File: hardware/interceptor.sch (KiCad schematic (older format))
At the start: 23 parts, among them IC1 ATMEGA1284P-P, P1 TAPEPORT, P2 CIA1, P3 KEYBOARD, P4 OUTPUT, U1 7400, U2 ICL7660, U3 4520, U4 4051, U5 4051, X1 16Mhz

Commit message: Hardware: Revised Design based on 8x8 Crosspoint Switch IC, Added USB
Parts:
- removed P4: OUTPUT, symbol CONN_12
- added C13: 100nF, ~, symbol C
- added C6: 100nF, symbol C
- added K1: USB, symbol CONN_3
- added P4: USER, symbol CONN_17
- added SW1: RESET, symbol SW_PUSH
- added SW2: BOOTLOADER, symbol SW_PUSH
- added U6: CD74HC22106, symbol CD74HC22106
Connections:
- net labels added: CPA0, CPA1, CPA2, CPA3, CPA4, CPA5, CPD, D+, D-, UA0, UA1, UA2, UA3, UA4, UA5, UA6, UA7, UB0, UB1, UB2, UB3, UB4, UB5, UB6, UB7, ~ATRES, ~CPE, ~CPS, ~HWBE
- net labels removed: GPO0, GPO1, GPO10, GPO11, GPO2, GPO3, GPO4, GPO5, GPO6, GPO7, GPO8, GPO9
- wire segments 23 -> 24
- no-connect marks 6 -> 5
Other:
- note added: "8x8 Crosspoint Switch"
- note added: "Connectors"
- note added: "Keyboard Scanner"
- note added: "Microcontroller"
- note added: "Negative Voltage Supply\n"
- note added: "Power-On-Reset\n"
- moved on the sheet: C1, C10, C11, C12, C2, C3, C4, C5, C7, C8, C9, IC1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

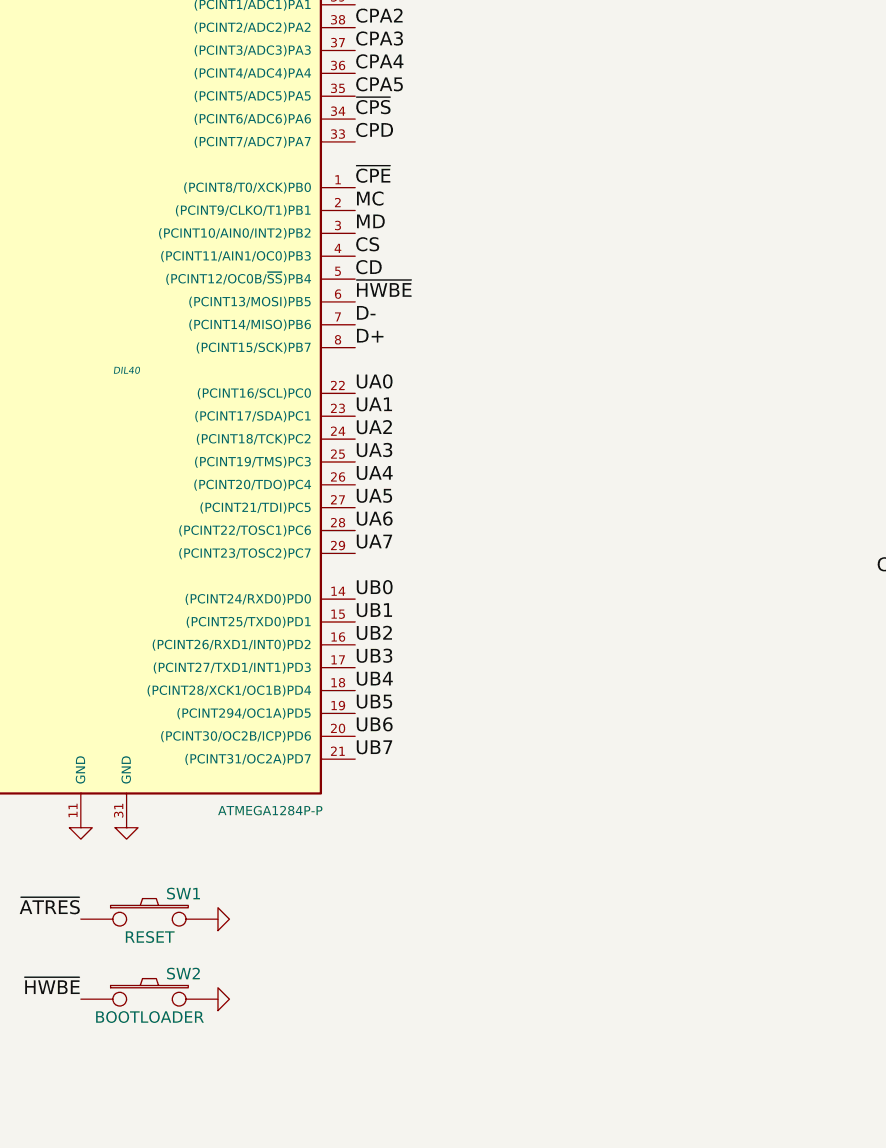
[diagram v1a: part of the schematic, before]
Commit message: Hardware: Added USB Level Conversion Diodes and Resistors
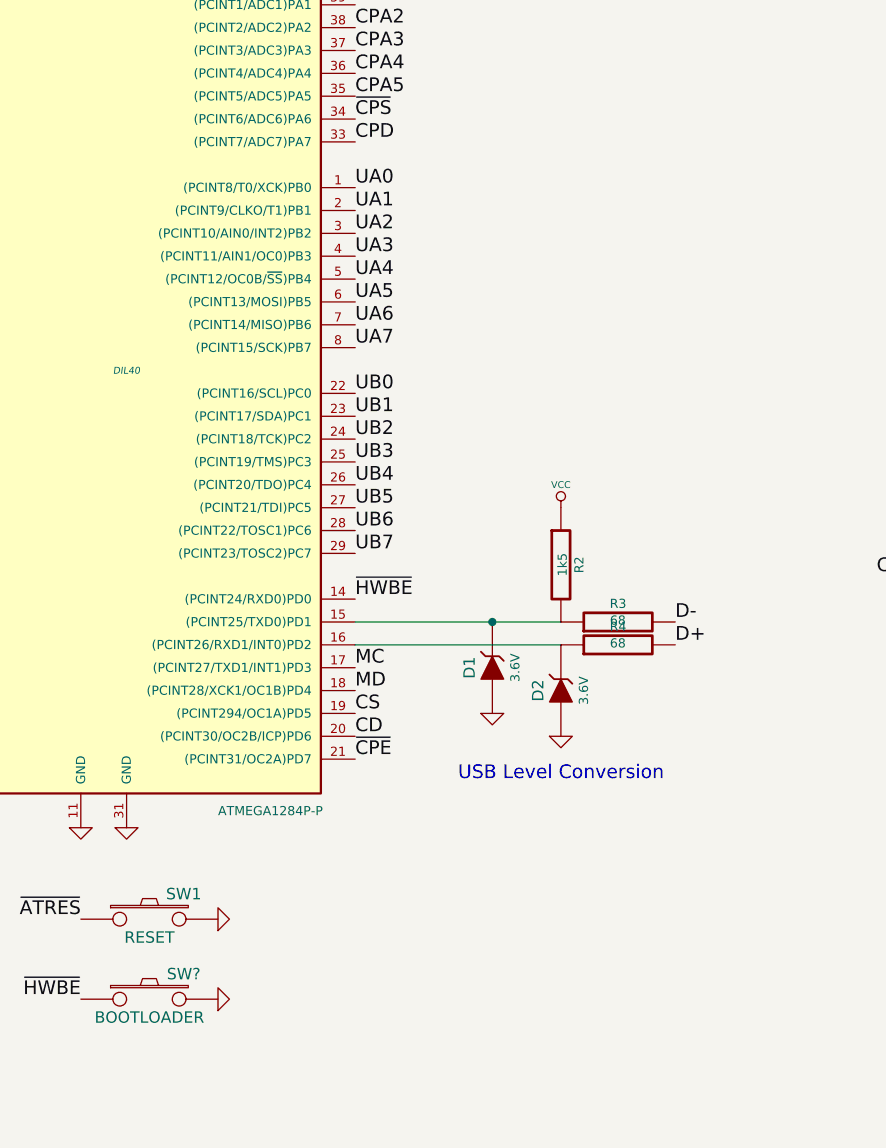
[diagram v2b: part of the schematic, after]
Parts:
- removed SW2: BOOTLOADER, symbol SW_PUSH
- added D1, D2: 3.6V, symbol ZENER
- added R2: 1k5, symbol R
- added R3, R4: 68, symbol R
- added SW?: BOOTLOADER, symbol SW_PUSH
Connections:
- net CD: now also IC1.20 ((PCINT30/OC2B/ICP)PD6); no longer IC1.5 ((PCINT12/OC0B/~SS~)PB4)
- net CS: now also IC1.19 ((PCINT294/OC1A)PD5); no longer IC1.4 ((PCINT11/AIN1/OC0)PB3)
- net D+: now also R4.2; no longer IC1.8 ((PCINT15/SCK)PB7)
- net D-: now also R3.2; no longer IC1.7 ((PCINT14/MISO)PB6)
- net GND: now also D1.1 (A), D2.1 (A), SW?.2
- net MC: now also IC1.17 ((PCINT27/TXD1/INT1)PD3); no longer IC1.2 ((PCINT9/CLKO/T1)PB1)
- net MD: now also IC1.18 ((PCINT28/XCK1/OC1B)PD4); no longer IC1.3 ((PCINT10/AIN0/INT2)PB2)
- net UA0: now also IC1.1 ((PCINT8/T0/XCK)PB0); no longer IC1.22 ((PCINT16/SCL)PC0)
- net UA1: now also IC1.2 ((PCINT9/CLKO/T1)PB1); no longer IC1.23 ((PCINT17/SDA)PC1)
- net UA2: now also IC1.3 ((PCINT10/AIN0/INT2)PB2); no longer IC1.24 ((PCINT18/TCK)PC2)
- net UA3: now also IC1.4 ((PCINT11/AIN1/OC0)PB3); no longer IC1.25 ((PCINT19/TMS)PC3)
- net UA4: now also IC1.5 ((PCINT12/OC0B/~SS~)PB4); no longer IC1.26 ((PCINT20/TDO)PC4)
- net UA5: now also IC1.6 ((PCINT13/MOSI)PB5); no longer IC1.27 ((PCINT21/TDI)PC5)
- net UA6: now also IC1.7 ((PCINT14/MISO)PB6); no longer IC1.28 ((PCINT22/TOSC1)PC6)
- net UA7: now also IC1.8 ((PCINT15/SCK)PB7); no longer IC1.29 ((PCINT23/TOSC2)PC7)
- net UB0: now also IC1.22 ((PCINT16/SCL)PC0); no longer IC1.14 ((PCINT24/RXD0)PD0)
- net UB1: now also IC1.23 ((PCINT17/SDA)PC1); no longer IC1.15 ((PCINT25/TXD0)PD1)
- net UB2: now also IC1.24 ((PCINT18/TCK)PC2); no longer IC1.16 ((PCINT26/RXD1/INT0)PD2)
- net UB3: now also IC1.25 ((PCINT19/TMS)PC3); no longer IC1.17 ((PCINT27/TXD1/INT1)PD3)
- net UB4: now also IC1.26 ((PCINT20/TDO)PC4); no longer IC1.18 ((PCINT28/XCK1/OC1B)PD4)
- net UB5: now also IC1.27 ((PCINT21/TDI)PC5); no longer IC1.19 ((PCINT294/OC1A)PD5)
- net UB6: now also IC1.28 ((PCINT22/TOSC1)PC6); no longer IC1.20 ((PCINT30/OC2B/ICP)PD6)
- net UB7: now also IC1.29 ((PCINT23/TOSC2)PC7); no longer IC1.21 ((PCINT31/OC2A)PD7)
- net VCC: now also R2.1
- net ~CPE: now also IC1.21 ((PCINT31/OC2A)PD7); no longer IC1.1 ((PCINT8/T0/XCK)PB0)
- net ~HWBE: now also IC1.14 ((PCINT24/RXD0)PD0), SW?.1; no longer IC1.6 ((PCINT13/MOSI)PB5)
- new net: D1.2 (K), IC1.15 ((PCINT25/TXD0)PD1), R2.2, R3.1
- new net: D2.2 (K), IC1.16 ((PCINT26/RXD1/INT0)PD2), R4.1
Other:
- note added: "USB Level Conversion\n"
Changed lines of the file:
@@
 Text Label 4850 5900 0    60   ~ 0
 B7
-Text Label 8900 4600 0    60   ~ 0
+Text Label 8900 6600 0    60   ~ 0
 MC
-Text Label 8900 4700 0    60   ~ 0
+Text Label 8900 6700 0    60   ~ 0
 MD
-Text Label 8900 4800 0    60   ~ 0
+Text Label 8900 6800 0    60   ~ 0
 CS
-Text Label 8900 4900 0    60   ~ 0
+Text Label 8900 6900 0    60   ~ 0
 CD
 Text Label 6900 4800 2    60   ~ 0
@@
 Text Label 8900 4300 0    60   ~ 0
 CPD
-Text Label 8900 4500 0    60   ~ 0
+Text Label 8900 7000 0    60   ~ 0
 ~CPE
-Text Label 8900 5000 0    60   ~ 0
-~HWBE
-$Comp
-L SW_PUSH SW2
-U 1 1 55B37A4E
-P 8000 8050
-F 0 "SW2" H 8150 8160 50  0000 C CNN
-F 1 "BOOTLOADER" H 8000 7970 50  0000 C CNN
-F 2 "" H 8000 8050 60  0000 C CNN
-F 3 "" H 8000 8050 60  0000 C CNN
-	1    8000 8050
-	1    0    0    -1
-$EndComp
 $Comp
 L GND #PWR044
@@
 	0    1    1    0
 $EndComp
+Text Label 10300 6400 0    60   ~ 0
+D-
+Text Label 10300 6500 0    60   ~ 0
+D+
+Text Label 8900 4500 0    60   ~ 0
+UA0
+Text Label 8900 4600 0    60   ~ 0
+UA1
+Text Label 8900 4700 0    60   ~ 0
+UA2
+Text Label 8900 4800 0    60   ~ 0
+UA3
+Text Label 8900 4900 0    60   ~ 0
+UA4
+Text Label 8900 5000 0    60   ~ 0
+UA5
 Text Label 8900 5100 0    60   ~ 0
-D-
+UA6
 Text Label 8900 5200 0    60   ~ 0
-D+
+UA7
 Text Label 8900 5400 0    60   ~ 0
-UA0
+UB0
 Text Label 8900 5500 0    60   ~ 0
-UA1
+UB1
 Text Label 8900 5600 0    60   ~ 0
-UA2
+UB2
 Text Label 8900 5700 0    60   ~ 0
-UA3
+UB3
 Text Label 8900 5800 0    60   ~ 0
-UA4
+UB4
 Text Label 8900 5900 0    60   ~ 0
-UA5
+UB5
 Text Label 8900 6000 0    60   ~ 0
-UA6
+UB6
 Text Label 8900 6100 0    60   ~ 0
-UA7
-Text Label 8900 6300 0    60   ~ 0
-UB0
-Text Label 8900 6400 0    60   ~ 0
-UB1
-Text Label 8900 6500 0    60   ~ 0
-UB2
-Text Label 8900 6600 0    60   ~ 0
-UB3
-Text Label 8900 6700 0    60   ~ 0
-UB4
-Text Label 8900 6800 0    60   ~ 0
-UB5
-Text Label 8900 6900 0    60   ~ 0
-UB6
-Text Label 8900 7000 0    60   ~ 0
 UB7
 $Comp
@@
 	1    0    0    -1
 $EndComp
+$Comp
+L R R3
+U 1 1 55B38786
+P 10050 6400
+F 0 "R3" V 10130 6400 40  0000 C CNN
+F 1 "68" V 10057 6401 40  0000 C CNN
+F 2 "" V 9980 6400 30  0000 C CNN
+F 3 "" H 10050 6400 30  0000 C CNN
+	1    10050 6400
+	0    -1   -1   0
+$EndComp
+$Comp
+L R R4
+U 1 1 55B38798
+P 10050 6500
+F 0 "R4" V 10130 6500 40  0000 C CNN
+F 1 "68" V 10057 6501 40  0000 C CNN
+F 2 "" V 9980 6500 30  0000 C CNN
+F 3 "" H 10050 6500 30  0000 C CNN
+	1    10050 6500
+	0    -1   -1   0
+$EndComp
+$Comp
+L R R2
+U 1 1 55B387AA
+P 9800 6150
+F 0 "R2" V 9880 6150 40  0000 C CNN
+F 1 "1k5" V 9807 6151 40  0000 C CNN
+F 2 "" V 9730 6150 30  0000 C CNN
+F 3 "" H 9800 6150 30  0000 C CNN
+	1    9800 6150
+	1    0    0    -1
+$EndComp
+$Comp
+L ZENER D2
+U 1 1 55B387CD
+P 9800 6700
+F 0 "D2" H 9800 6800 50  0000 C CNN
+F 1 "3.6V" H 9800 6600 40  0000 C CNN
+F 2 "" H 9800 6700 60  0000 C CNN
+F 3 "" H 9800 6700 60  0000 C CNN
+	1    9800 6700
+	0    -1   -1   0
+$EndComp
+$Comp
+L ZENER D1
+U 1 1 55B387E1
+P 9500 6600
+F 0 "D1" H 9500 6700 50  0000 C CNN
+F 1 "3.6V" H 9500 6500 40  0000 C CNN
+F 2 "" H 9500 6600 60  0000 C CNN
+F 3 "" H 9500 6600 60  0000 C CNN
+	1    9500 6600
+	0    -1   -1   0
+$EndComp
+$Comp
+L VCC #PWR050
+U 1 1 55B387FF
+P 9800 5900
+F 0 "#PWR050" H 9800 6000 30  0001 C CNN
+F 1 "VCC" H 9800 6000 30  0000 C CNN
+F 2 "" H 9800 5900 60  0000 C CNN
+F 3 "" H 9800 5900 60  0000 C CNN
+	1    9800 5900
+	1    0    0    -1
+$EndComp
+$Comp
+L GND #PWR051
+U 1 1 55B38813
+P 9800 6900
+F 0 "#PWR051" H 9800 6900 30  0001 C CNN
+F 1 "GND" H 9800 6830 30  0001 C CNN
+F 2 "" H 9800 6900 60  0000 C CNN
+F 3 "" H 9800 6900 60  0000 C CNN
+	1    9800 6900
+	1    0    0    -1
+$EndComp
+$Comp
+L GND #PWR052
+U 1 1 55B38825
+P 9500 6800
+F 0 "#PWR052" H 9500 6800 30  0001 C CNN
+F 1 "GND" H 9500 6730 30  0001 C CNN
+F 2 "" H 9500 6800 60  0000 C CNN
+F 3 "" H 9500 6800 60  0000 C CNN
+	1    9500 6800
+	1    0    0    -1
+$EndComp
+Text Notes 9350 7100 0    60   ~ 0
+USB Level Conversion\n
+Text Label 8900 6300 0    60   ~ 0
+~HWBE
+Wire Wire Line
+	8900 6400 9800 6400
+Connection ~ 9500 6400
+Wire Wire Line
+	8900 6500 9800 6500
+$Comp
+L SW_PUSH SW?
+U 1 1 55B3E8F4
+P 8000 8050
+F 0 "SW?" H 8150 8160 50  0000 C CNN
+F 1 "BOOTLOADER" H 8000 7970 50  0000 C CNN
+F 2 "" H 8000 8050 60  0000 C CNN
+F 3 "" H 8000 8050 60  0000 C CNN
+	1    8000 8050
+	1    0    0    -1
+$EndComp

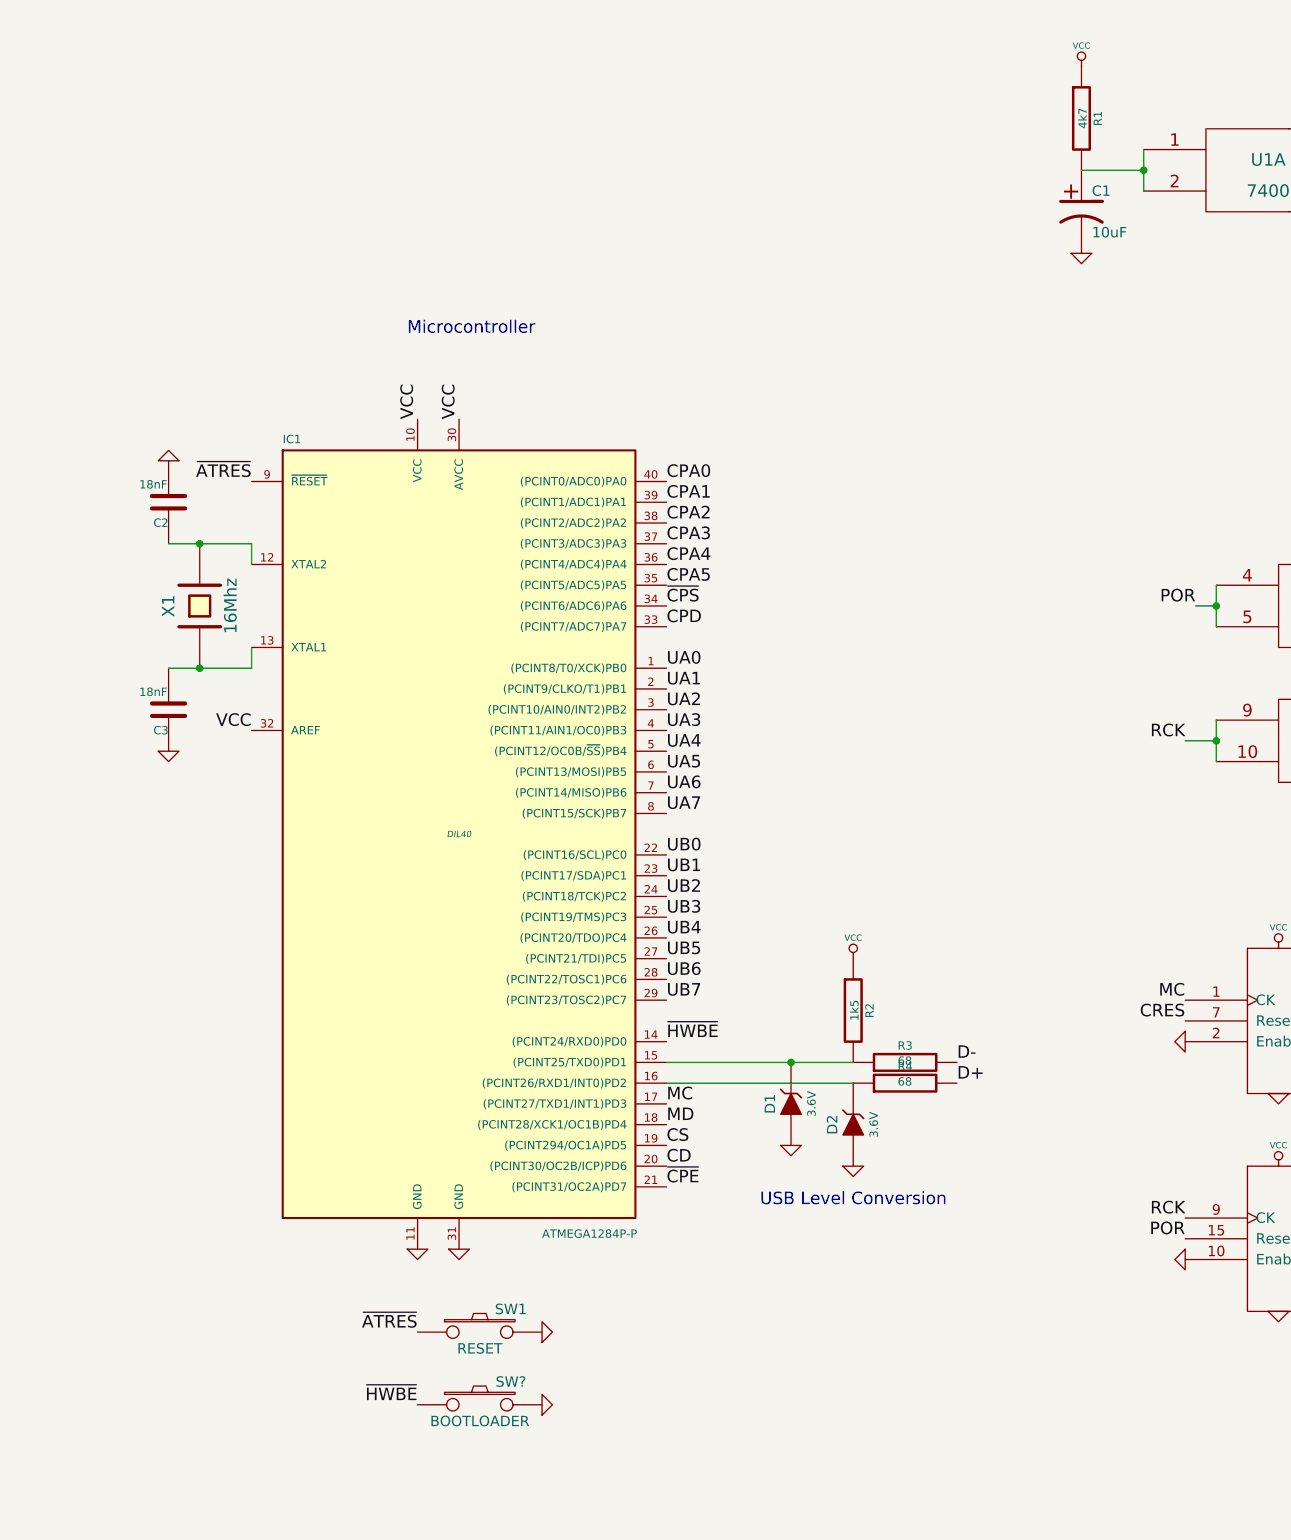
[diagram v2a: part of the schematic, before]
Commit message: Hardware: Trigger power-on-reset when pushing reset switch
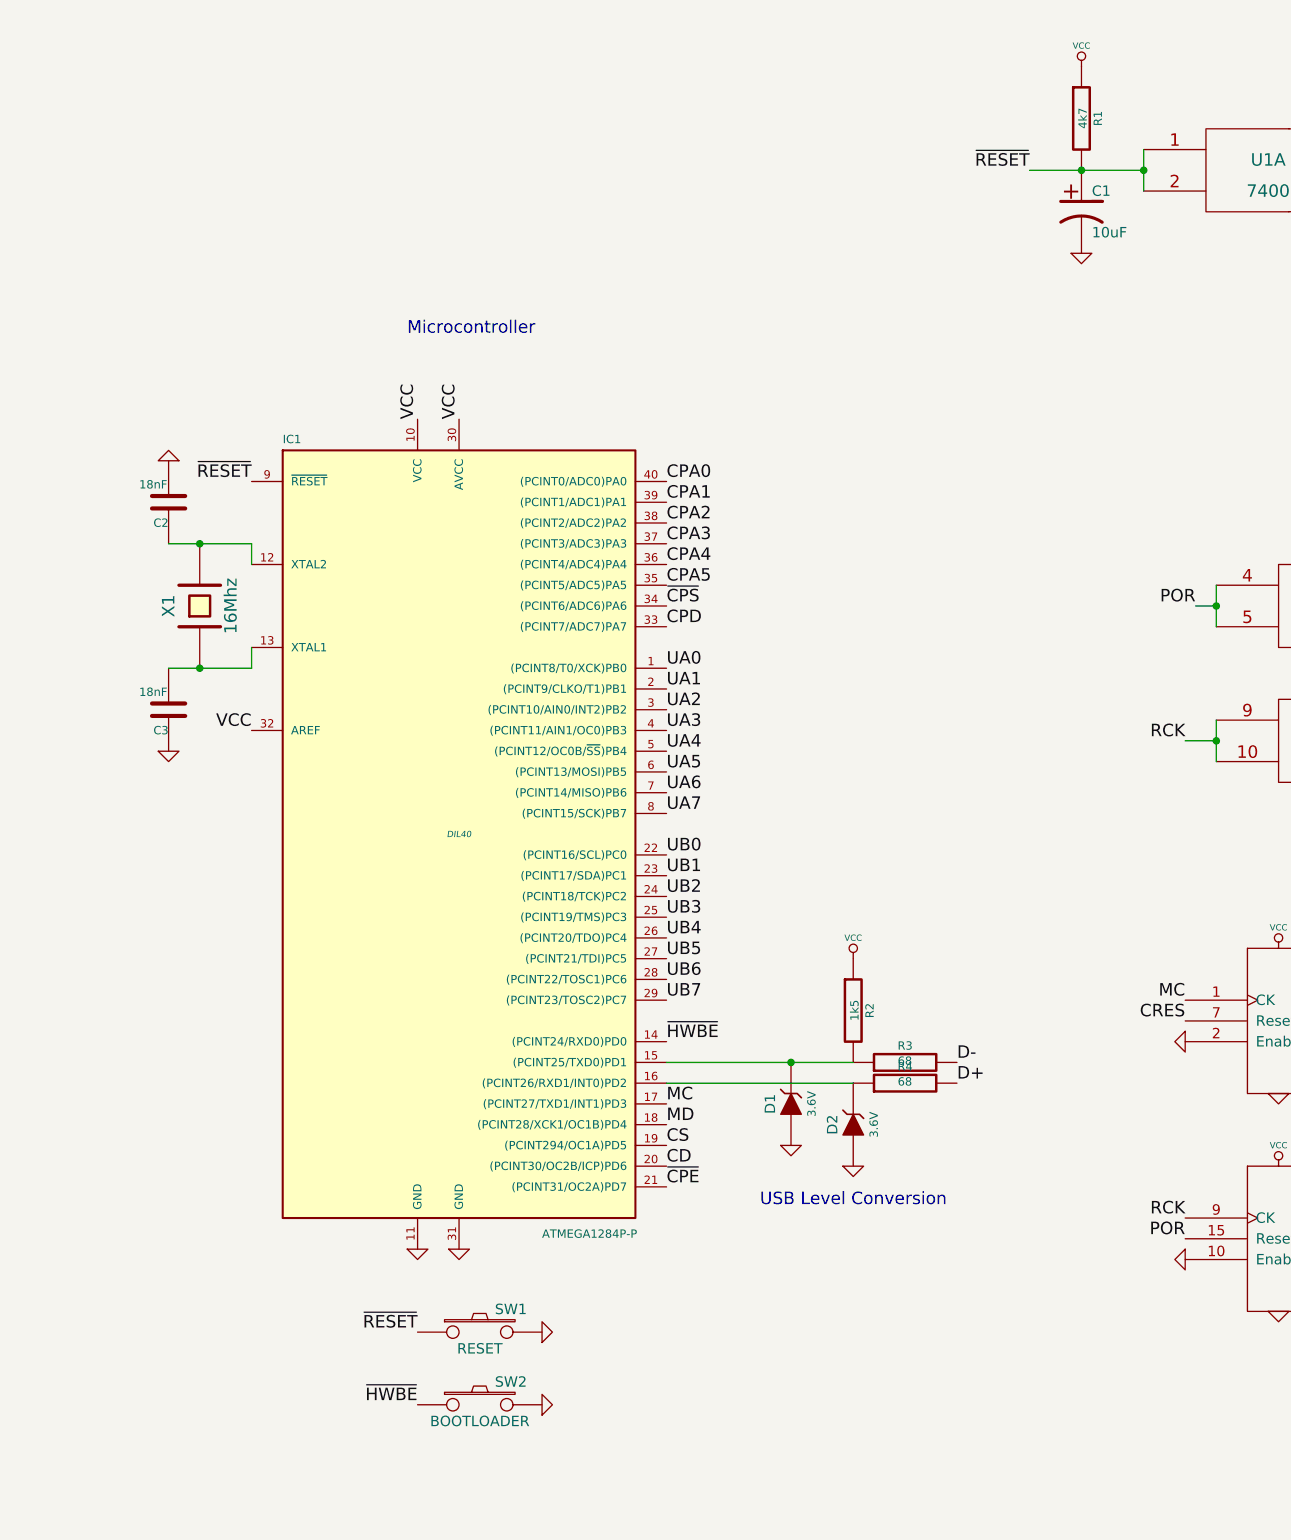
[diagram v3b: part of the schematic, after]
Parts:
- gave numbers to parts that had none: 1
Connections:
- net ~ATRES is gone; now on net ~RESET: IC1.9 (~RESET), SW1.1
- net ~RESET: now reaches C1.1, R1.2, U1.1, U1.2
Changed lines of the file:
@@
 	11200 2000 11200 2200
 Wire Wire Line
-	10900 2100 11200 2100
+	10650 2100 11200 2100
 Connection ~ 11200 2100
 $Comp
@@
 $EndComp
 Text Label 7700 7700 2    60   ~ 0
-~ATRES
+~RESET
 Text Label 6900 3600 2    60   ~ 0
-~ATRES
+~RESET
 $Comp
 L CONN_3 K1
@@
 	8900 6500 9800 6500
 $Comp
-L SW_PUSH SW?
+L SW_PUSH SW2
 U 1 1 55B3E8F4
 P 8000 8050
-F 0 "SW?" H 8150 8160 50  0000 C CNN
+F 0 "SW2" H 8150 8160 50  0000 C CNN
 F 1 "BOOTLOADER" H 8000 7970 50  0000 C CNN
 F 2 "" H 8000 8050 60  0000 C CNN
@@
 	1    0    0    -1
 $EndComp
+Text Label 10650 2100 2    60   ~ 0
+~RESET
+Connection ~ 10900 2100
 $EndSCHEMATC
